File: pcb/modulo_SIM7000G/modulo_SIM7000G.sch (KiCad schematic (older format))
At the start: 58 parts, among them J1 Conn_01x04, J2 115Q-BCA0, J3 INTERFAZ SERIAL, J4 Conn_01x02, J5 DCJ200-10-A-XX-X_REVA, J6 1661, J7 1661, Q1 NTE4153NT1G, Q2 NTE4153NT1G, Q3 NTE4153NT1G, U1 SIM7000G, U2 SN74LV1T34DCKR, U3 SN74LV1T34DCKR, U4 SN74LV1T34DCKR, U5 SN74LV1T34DCKR, U6 SN74LV1T34DCKR, U7 MIC29302WU, U8 LM1117-3.3

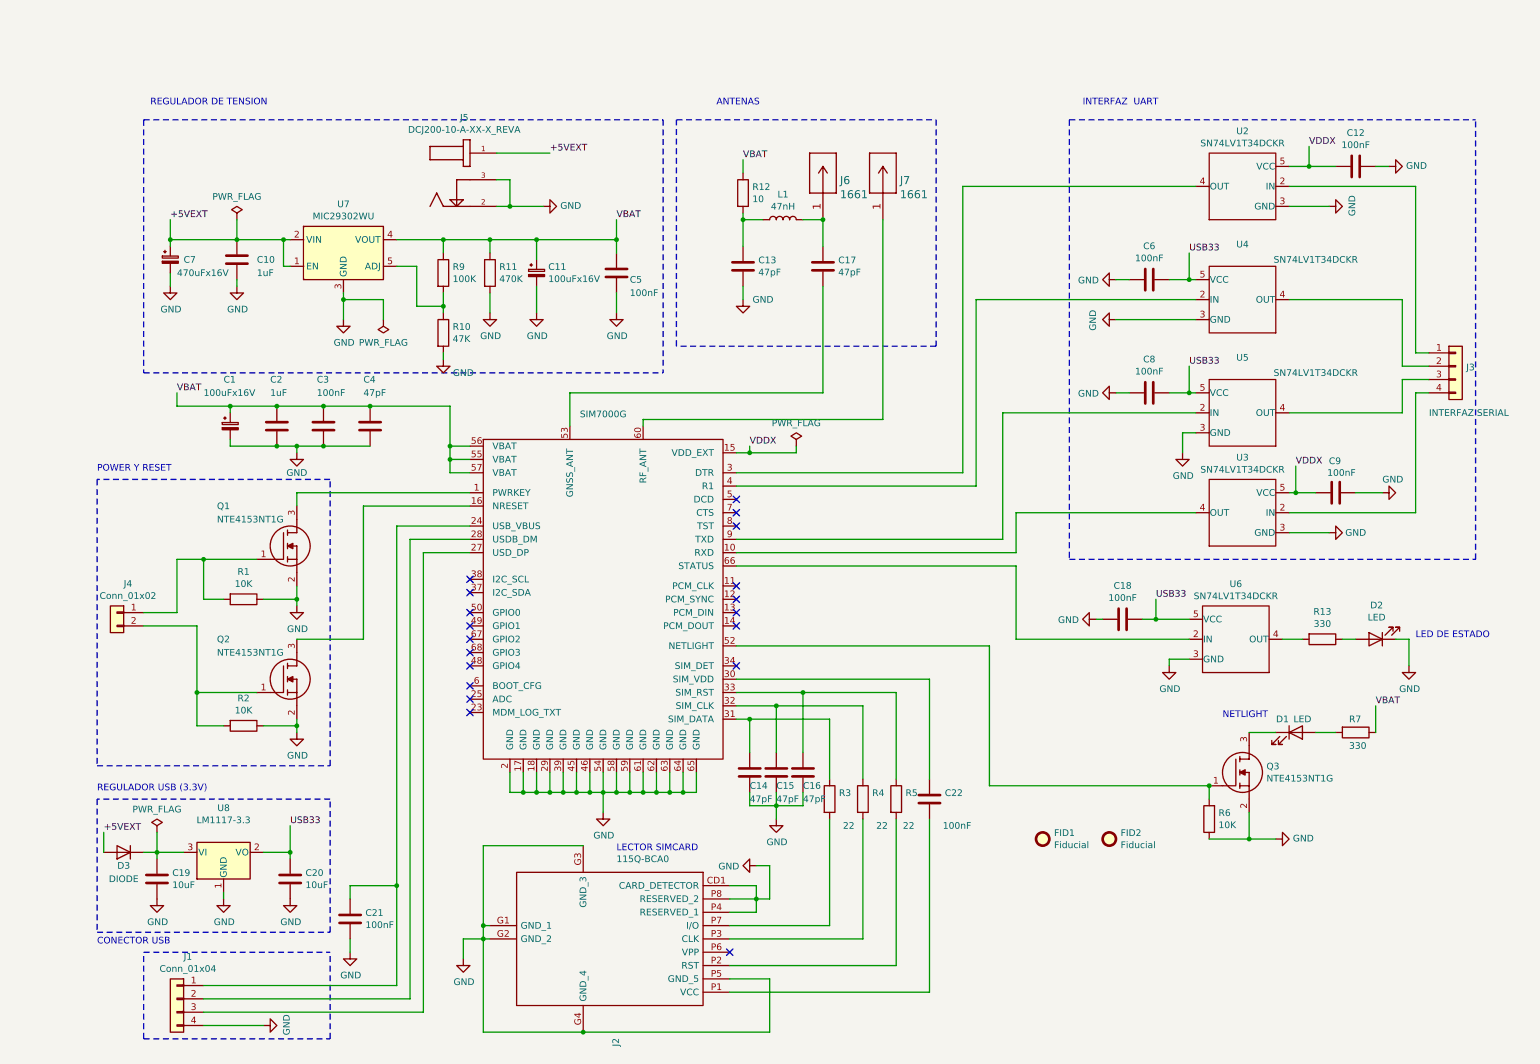
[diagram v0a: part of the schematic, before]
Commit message: correciones en el esquematico, se agrego agujeros de montaje
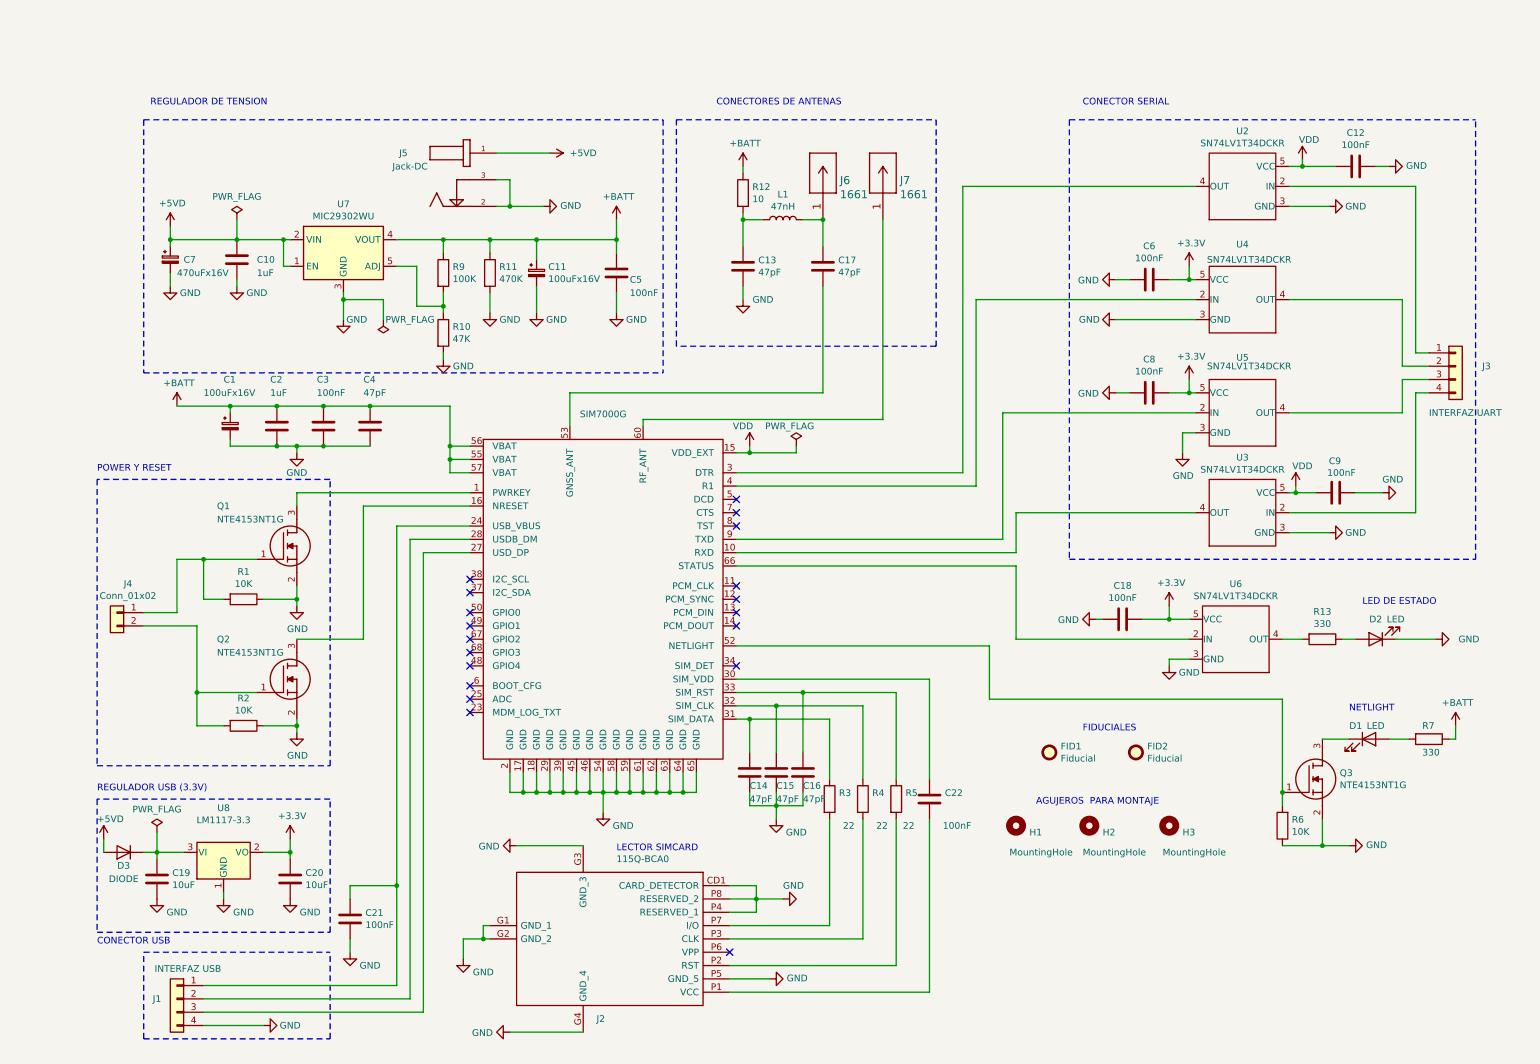
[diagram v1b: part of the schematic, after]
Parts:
- added H1, H2, H3: MountingHole, MountingHole:MountingHole_2.2mm_M2_ISO7380_Pad_TopBottom, symbol Mechanical:MountingHole
- J1: value Conn_01x04 -> INTERFAZ USB
- J3: value INTERFAZ SERIAL -> INTERFAZ UART
- J5: value DCJ200-10-A-XX-X_REVA -> Jack-DC
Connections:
- net +5VEXT renamed +5VD
- net USB33 renamed +3V3
- net VBAT renamed +BATT
- net VDDX renamed VDD
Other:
- note added: "AGUJEROS PARA MONTAJE"
- note added: "CONECTOR SERIAL"
- note added: "CONECTORES DE ANTENAS"
- note added: "FIDUCIALES"
- note removed: "ANTENAS"
- note removed: "INTERFAZ UART"
- moved on the sheet: D1, FID1, FID2, Q3, R6, R7

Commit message: antes de empezar el diseño de las pistas
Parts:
- Q1, Q2, Q3: symbol NTE4153NT1G:NTE4153NT1G -> modulo_SIM7000G-rescue:NTE4153NT1G-NTE4153NT1G
- U1: symbol RF_GSM:SIM7000G -> modulo_SIM7000G-rescue:SIM7000G-RF_GSM
- U2, U3, U4, U5, U6: symbol SN74LV1T34DCKR:SN74LV1T34DCKR -> modulo_SIM7000G-rescue:SN74LV1T34DCKR-SN74LV1T34DCKR
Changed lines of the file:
@@
 $EndDescr
 $Comp
-L NTE4153NT1G:NTE4153NT1G Q2
+L modulo_SIM7000G-rescue:NTE4153NT1G-NTE4153NT1G Q2
 U 1 1 6146EC82
 P 1750 5150
@@
 $EndComp
 $Comp
-L NTE4153NT1G:NTE4153NT1G Q1
+L modulo_SIM7000G-rescue:NTE4153NT1G-NTE4153NT1G Q1
 U 1 1 6146A9EB
 P 1750 4150
@@
 	1350 7350 2800 7350
 $Comp
-L SN74LV1T34DCKR:SN74LV1T34DCKR U5
+L modulo_SIM7000G-rescue:SN74LV1T34DCKR-SN74LV1T34DCKR U5
 U 1 1 6152D798
 P 9200 3000
@@
 CONECTORES DE ANTENAS
 $Comp
-L SN74LV1T34DCKR:SN74LV1T34DCKR U4
+L modulo_SIM7000G-rescue:SN74LV1T34DCKR-SN74LV1T34DCKR U4
 U 1 1 6153062F
 P 9200 2150
@@
 CONECTOR SERIAL
 $Comp
-L SN74LV1T34DCKR:SN74LV1T34DCKR U3
+L modulo_SIM7000G-rescue:SN74LV1T34DCKR-SN74LV1T34DCKR U3
 U 1 1 61522A68
 P 9100 3750
@@
 $EndComp
 $Comp
-L SN74LV1T34DCKR:SN74LV1T34DCKR U6
+L modulo_SIM7000G-rescue:SN74LV1T34DCKR-SN74LV1T34DCKR U6
 U 1 1 6150BE97
 P 9150 4700
@@
 	5850 5900 5850 6000
 $Comp
-L RF_GSM:SIM7000G U1
+L modulo_SIM7000G-rescue:SIM7000G-RF_GSM U1
 U 1 1 614D3DBD
 P -6200 -4000
@@
 	8600 2900 8750 2900
 $Comp
-L SN74LV1T34DCKR:SN74LV1T34DCKR U2
+L modulo_SIM7000G-rescue:SN74LV1T34DCKR-SN74LV1T34DCKR U2
 U 1 1 61593BF9
 P 9100 1300
@@
 	9750 6100 9750 6300
 $Comp
-L NTE4153NT1G:NTE4153NT1G Q3
+L modulo_SIM7000G-rescue:NTE4153NT1G-NTE4153NT1G Q3
 U 1 1 6143BDA3
 P 9450 5900

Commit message: se termino de diseñar las pistas. Falta plano de alimentacion y detalles
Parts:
- removed C21: 100nF, Capacitor_SMD:C_0805_2012Metric_Pad1.18x1.45mm_HandSolder, symbol Device:C
- removed J1: INTERFAZ USB, Connector_PinHeader_2.00mm:PinHeader_1x04_P2.00mm_Vertical, symbol Connector_Generic:Conn_01x04
- removed J3: INTERFAZ UART, Connector:FanPinHeader_1x04_P2.54mm_Vertical, symbol Connector_Generic:Conn_01x04
- removed J4: Conn_01x02, Connector_PinHeader_2.00mm:PinHeader_1x02_P2.00mm_Vertical, symbol Connector_Generic:Conn_01x02
- added J1: Conector Serial, Connector_PinHeader_2.54mm:PinHeader_1x06_P2.54mm_Horizontal, symbol Connector_Generic:Conn_01x06
- J2: symbol modulo_SIM7000G-rescue:115Q-BCA0-115Q-BCA0 -> modulo_SIM7000G-rescue:115Q-BCA0-115Q-BCA0-modulo_SIM7000G-rescue; TEM (none) -> https://www.tme.eu/es/details/115q-bca0/conectores-de-tarje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
- J5: symbol modulo_SIM7000G-rescue:DCJ200-10-A-XX-X_REVA-DCJ200-10-A-XX-X_REVA -> modulo_SIM7000G-rescue:DCJ200-10-A-XX-X_REVA-DCJ200-10-A-XX-X_REVA-modulo_SIM7000G-rescue
- J6, J7: footprint conn_ufl:1661 -> Connector_Coaxial:U.FL_Molex_MCRF_73412-0110_Vertical; symbol modulo_SIM7000G-rescue:1661-conn_ufl -> modulo_SIM7000G-rescue:1661-conn_ufl-modulo_SIM7000G-rescue
- Q1, Q2: symbol modulo_SIM7000G-rescue:NTE4153NT1G-NTE4153NT1G -> modulo_SIM7000G-rescue:NTE4153NT1G-NTE4153NT1G-modulo_SIM7000G-rescue; Digikey (none) -> NTE4153NT1GOSTR-ND
- Q3: symbol modulo_SIM7000G-rescue:NTE4153NT1G-NTE4153NT1G -> modulo_SIM7000G-rescue:NTE4153NT1G-NTE4153NT1G-modulo_SIM7000G-rescue
- U1: footprint RF_GSM:SIM7000 -> SIM7000G:SIM7000; symbol modulo_SIM7000G-rescue:SIM7000G-RF_GSM -> modulo_SIM7000G-rescue:SIM7000G-RF_GSM-modulo_SIM7000G-rescue; Descripcion (none) -> Módulo de comunicación Celular 4G (NB-IoT & CAT.M1) y GSM/G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
- U2, U3, U4, U5, U6: symbol modulo_SIM7000G-rescue:SN74LV1T34DCKR-SN74LV1T34DCKR -> modulo_SIM7000G-rescue:SN74LV1T34DCKR-SN74LV1T34DCKR-modulo_SIM7000G-rescue
- U7: Description (none) -> PMIC - reguladores de voltaje lineal Positivo Ajuste 1 Sali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; Digikey (none) -> 576-1125-2-NDTR
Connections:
- net POWERKEY: now reaches Q1.1, R1.2
- net POWERKEY: now also J1.6 (Pin_6)
- net NRESET: now reaches Q2.1, R2.2
- net NRESET: now also J1.1 (Pin_1)
- net at U1.30 (SIM_VDD): now also C22.2; no longer C22.1
- net at C15.1, U1.32 (SIM_CLK): now also R5.2; no longer R4.1
- net at J2.P1 (VCC): now also C22.1; no longer C22.2
- net at J2.P2 (RST): now also R4.1; no longer R5.2
- net at R4.2: now also C14.1, U1.33 (SIM_RST); no longer J2.P3 (CLK)
- net at R3.2: now also C16.1, U1.31 (SIM_DATA); no longer J2.P7 (I/O)
- net RX: now reaches U3.2 (IN)
- net RX: now also J1.2 (Pin_2)
- net TX: now reaches U5.4 (OUT)
- net TX: now also J1.3 (Pin_3)
- net RI: now reaches U4.4 (OUT)
- net RI: now also J1.4 (Pin_4)
- net DTR: now reaches U2.2 (IN)
- net DTR: now also J1.5 (Pin_5)
- new net: J2.P3 (CLK), R5.1
- new net: J2.P7 (I/O), R3.1
- no-connect marks 19 -> 22
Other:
- note added: "INTERFAZ SERIAL"
- note added: "JACK 5V"
- note added: "REGULADOR 3.3V"
- note added: "REGULADOR PARA BATERIA"
- note removed: "CONECTOR SERIAL"
- note removed: "CONECTOR USB"
- note removed: "REGULADOR DE TENSION"
- note removed: "REGULADOR USB (3.3V)"
- moved on the sheet: C1, C10, C11, C12, C13, C14, C15, C16, C17, C18, C19, C2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
